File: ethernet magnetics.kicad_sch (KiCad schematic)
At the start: 3 parts

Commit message: wired phy controller
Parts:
- removed U?: ALANS10001-4J41ET, symbol local_library:ALANS10001-4J41ET
- added C? (x2): 6.8nF, symbol Device:C
- added C? (x2): 0.022uF, symbol Device:C
- added C?: 0.01uF, symbol Device:C
- added C?: 3.3uF, symbol Device:C_Polarized
- added C?: 1000pf, symbol Device:C
- added FB?: FerriteBead, symbol Device:FerriteBead
- added R? (x4): 49.9, symbol Device:R
- added R? (x2): 150R, symbol Device:R
- added R?: 10, symbol Device:R
- added T?: S558-5999-46-F, SOP254P1270X597-16N, symbol SamacSys_Parts:S558-5999-46-F
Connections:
- net ETH-RXn: now also R?.1, T?.6
- net ETH-RXp: now also R?.1, T?.7
- net ETH-TXn: now also T?.11
- net ETH-TXp: now also T?.10
- net MAG-RXn: now also C?.1, R?.1
- net MAG-RXp: now also C?.1, R?.1
- net MAG-TXn: now also R?.2, T?.15
- net MAG-TXp: now also R?.2, T?.16
- net at R?.1: now also T?.5
- net at R?.1: now also R?.2, C?.1, R?.2, R?.2
- net ETH-GND: no longer names the net of R?.2
- net ETH-GND: now also T?.12; no longer R?.2
- new net: C?.2, T?.1
- new net: C?.1, R?.2, R?.2, T?.3
- new net: C?.1, C?.1, FB?.2, R?.1, R?.1, R?.1
- new net: C?.1, R?.2, T?.14
- new net: C?.2, T?.2
- new net +3V3: FB?.1
- new net GND: C?.2, C?.2, C?.2, C?.2
- new net GND1: C?.2
- no-connect marks 0 -> 4
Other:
- moved on the sheet: R?

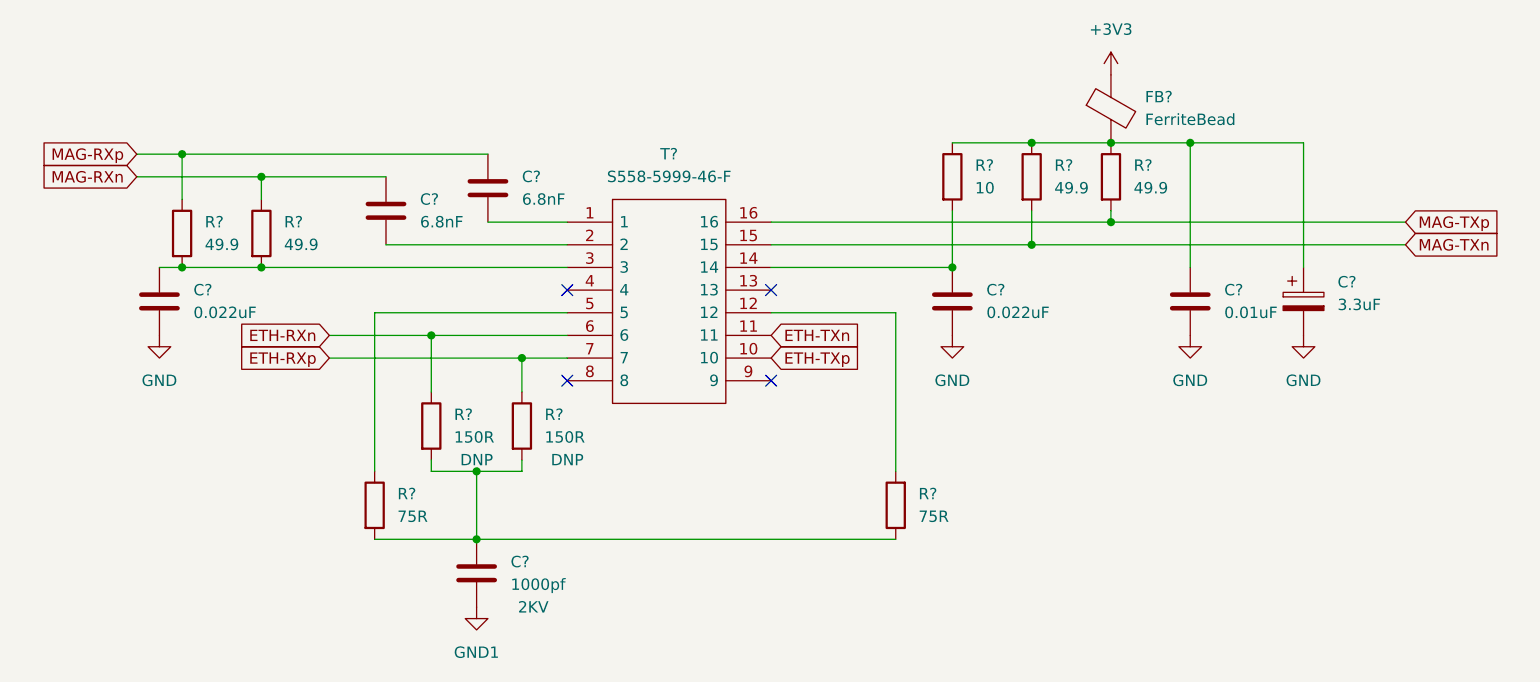
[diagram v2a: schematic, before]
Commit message: add component numbers to schematic
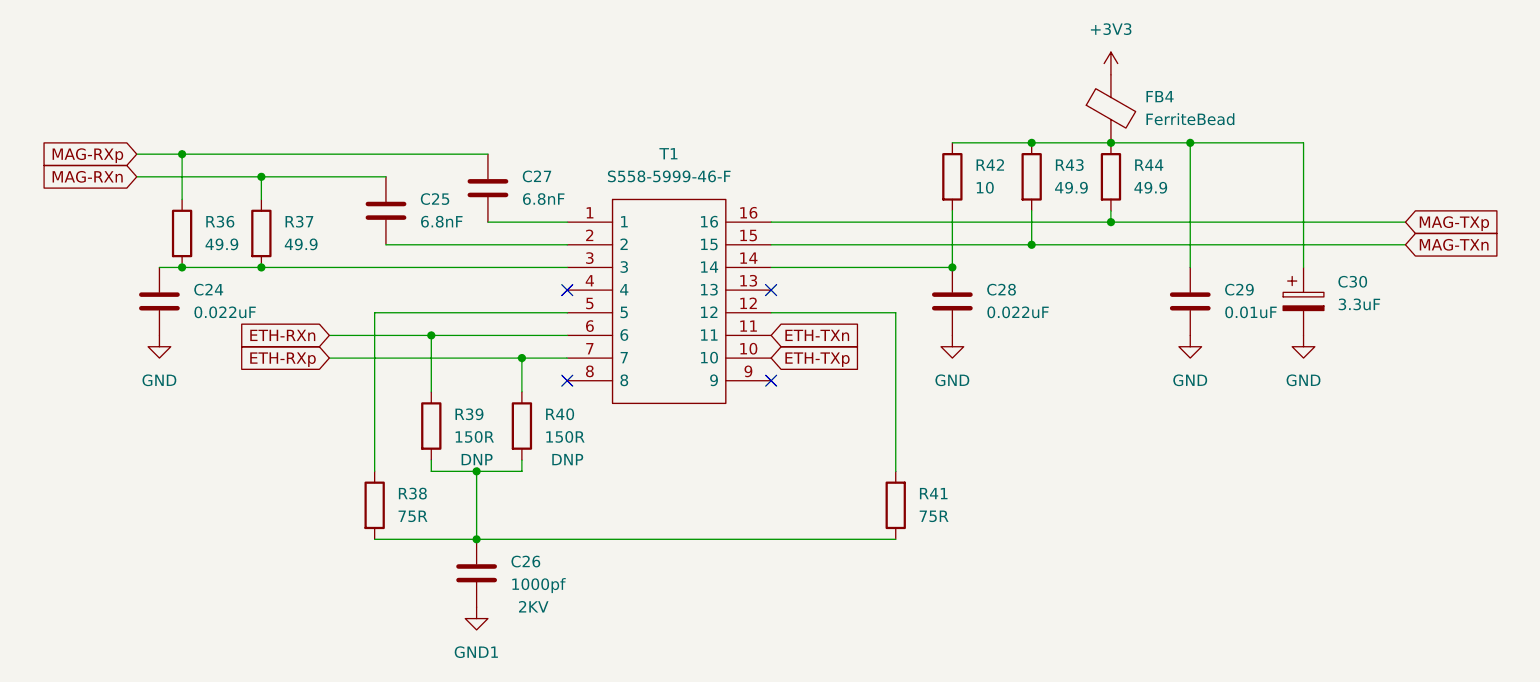
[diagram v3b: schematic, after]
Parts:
- gave numbers to parts that had none: 18
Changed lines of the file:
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@@
   (symbol (lib_id "power:GND") (at 199.39 85.09 0) (unit 1)
     (in_bom yes) (on_board yes) (fields_autoplaced)
-    (property "Reference" "#PWR?" (id 0) (at 199.39 91.44 0)
+    (property "Reference" "#PWR045" (id 0) (at 199.39 91.44 0)
       (effects (font (size 1.27 1.27)) hide)
     )
@@
   (symbol (lib_id "Device:C") (at 107.95 68.58 0) (unit 1)
     (in_bom yes) (on_board yes) (fields_autoplaced)
-    (property "Reference" "C?" (id 0) (at 111.76 67.3099 0)
+    (property "Reference" "C27" (id 0) (at 111.76 67.3099 0)
       (effects (font (size 1.27 1.27)) (justify left))
     )
@@
   (symbol (lib_id "Device:R") (at 95.25 104.14 0) (unit 1)
     (in_bom yes) (on_board yes) (fields_autoplaced)
-    (property "Reference" "R?" (id 0) (at 97.79 102.8699 0)
+    (property "Reference" "R38" (id 0) (at 97.79 102.8699 0)
       (effects (font (size 1.27 1.27)) (justify left))
     )
@@
   (symbol (lib_id "Device:C") (at 71.12 81.28 0) (unit 1)
     (in_bom yes) (on_board yes) (fields_autoplaced)
-    (property "Reference" "C?" (id 0) (at 74.93 80.0099 0)
+    (property "Reference" "C24" (id 0) (at 74.93 80.0099 0)
       (effects (font (size 1.27 1.27)) (justify left))
     )
@@
   (symbol (lib_id "Device:R") (at 177.8 67.31 0) (unit 1)
     (in_bom yes) (on_board yes) (fields_autoplaced)
-    (property "Reference" "R?" (id 0) (at 180.34 66.0399 0)
+    (property "Reference" "R44" (id 0) (at 180.34 66.0399 0)
       (effects (font (size 1.27 1.27)) (justify left))
     )
@@
   (symbol (lib_id "power:GND") (at 186.69 85.09 0) (unit 1)
     (in_bom yes) (on_board yes) (fields_autoplaced)
-    (property "Reference" "#PWR?" (id 0) (at 186.69 91.44 0)
+    (property "Reference" "#PWR044" (id 0) (at 186.69 91.44 0)
       (effects (font (size 1.27 1.27)) hide)
     )
@@
   (symbol (lib_id "Device:R") (at 73.66 73.66 0) (unit 1)
     (in_bom yes) (on_board yes) (fields_autoplaced)
-    (property "Reference" "R?" (id 0) (at 76.2 72.3899 0)
+    (property "Reference" "R36" (id 0) (at 76.2 72.3899 0)
       (effects (font (size 1.27 1.27)) (justify left))
     )
@@
   (symbol (lib_id "SamacSys_Parts:S558-5999-46-F") (at 116.84 72.39 0) (unit 1)
     (in_bom yes) (on_board yes) (fields_autoplaced)
-    (property "Reference" "T?" (id 0) (at 128.27 64.77 0))
+    (property "Reference" "T1" (id 0) (at 128.27 64.77 0))
     (property "Value" "S558-5999-46-F" (id 1) (at 128.27 67.31 0))
     (property "Footprint" "SOP254P1270X597-16N" (id 2) (at 135.89 69.85 0)
@@
   (symbol (lib_id "Device:C") (at 186.69 81.28 0) (unit 1)
     (in_bom yes) (on_board yes) (fields_autoplaced)
-    (property "Reference" "C?" (id 0) (at 190.5 80.0099 0)
+    (property "Reference" "C29" (id 0) (at 190.5 80.0099 0)
       (effects (font (size 1.27 1.27)) (justify left))
     )
@@
   (symbol (lib_id "Device:R") (at 111.76 95.25 0) (unit 1)
     (in_bom yes) (on_board yes)
-    (property "Reference" "R?" (id 0) (at 114.3 93.9799 0)
+    (property "Reference" "R40" (id 0) (at 114.3 93.9799 0)
       (effects (font (size 1.27 1.27)) (justify left))
     )
@@
   (symbol (lib_id "Device:R") (at 82.55 73.66 0) (unit 1)
     (in_bom yes) (on_board yes) (fields_autoplaced)
-    (property "Reference" "R?" (id 0) (at 85.09 72.3899 0)
+    (property "Reference" "R37" (id 0) (at 85.09 72.3899 0)
       (effects (font (size 1.27 1.27)) (justify left))
     )
@@
   (symbol (lib_id "Device:R") (at 168.91 67.31 0) (unit 1)
     (in_bom yes) (on_board yes) (fields_autoplaced)
-    (property "Reference" "R?" (id 0) (at 171.45 66.0399 0)
+    (property "Reference" "R43" (id 0) (at 171.45 66.0399 0)
       (effects (font (size 1.27 1.27)) (justify left))
     )
@@
   (symbol (lib_id "Device:C_Polarized") (at 199.39 81.28 0) (unit 1)
     (in_bom yes) (on_board yes) (fields_autoplaced)
-    (property "Reference" "C?" (id 0) (at 203.2 79.1209 0)
+    (property "Reference" "C30" (id 0) (at 203.2 79.1209 0)
       (effects (font (size 1.27 1.27)) (justify left))
     )
@@
   (symbol (lib_id "power:GND") (at 160.02 85.09 0) (unit 1)
     (in_bom yes) (on_board yes) (fields_autoplaced)
-    (property "Reference" "#PWR?" (id 0) (at 160.02 91.44 0)
+    (property "Reference" "#PWR042" (id 0) (at 160.02 91.44 0)
       (effects (font (size 1.27 1.27)) hide)
     )
@@
   (symbol (lib_id "power:+3V3") (at 177.8 55.88 0) (unit 1)
     (in_bom yes) (on_board yes) (fields_autoplaced)
-    (property "Reference" "#PWR?" (id 0) (at 177.8 59.69 0)
+    (property "Reference" "#PWR043" (id 0) (at 177.8 59.69 0)
       (effects (font (size 1.27 1.27)) hide)
     )
@@
   (symbol (lib_id "Device:R") (at 153.67 104.14 180) (unit 1)
     (in_bom yes) (on_board yes) (fields_autoplaced)
-    (property "Reference" "R?" (id 0) (at 156.21 102.8699 0)
+    (property "Reference" "R41" (id 0) (at 156.21 102.8699 0)
       (effects (font (size 1.27 1.27)) (justify right))
     )
@@
   (symbol (lib_id "Device:C") (at 96.52 71.12 0) (unit 1)
     (in_bom yes) (on_board yes) (fields_autoplaced)
-    (property "Reference" "C?" (id 0) (at 100.33 69.8499 0)
+    (property "Reference" "C25" (id 0) (at 100.33 69.8499 0)
       (effects (font (size 1.27 1.27)) (justify left))
     )
@@
   (symbol (lib_id "Device:C") (at 160.02 81.28 0) (unit 1)
     (in_bom yes) (on_board yes) (fields_autoplaced)
-    (property "Reference" "C?" (id 0) (at 163.83 80.0099 0)
+    (property "Reference" "C28" (id 0) (at 163.83 80.0099 0)
       (effects (font (size 1.27 1.27)) (justify left))
     )
@@
   (symbol (lib_id "power:GND") (at 71.12 85.09 0) (unit 1)
     (in_bom yes) (on_board yes) (fields_autoplaced)
-    (property "Reference" "#PWR?" (id 0) (at 71.12 91.44 0)
+    (property "Reference" "#PWR040" (id 0) (at 71.12 91.44 0)
       (effects (font (size 1.27 1.27)) hide)
     )
@@
   (symbol (lib_id "Device:R") (at 101.6 95.25 0) (unit 1)
     (in_bom yes) (on_board yes)
-    (property "Reference" "R?" (id 0) (at 104.14 93.9799 0)
+    (property "Reference" "R39" (id 0) (at 104.14 93.9799 0)
       (effects (font (size 1.27 1.27)) (justify left))
     )
@@
   (symbol (lib_id "power:GND1") (at 106.68 115.57 0) (unit 1)
     (in_bom yes) (on_board yes) (fields_autoplaced)
-    (property "Reference" "#PWR?" (id 0) (at 106.68 121.92 0)
+    (property "Reference" "#PWR041" (id 0) (at 106.68 121.92 0)
       (effects (font (size 1.27 1.27)) hide)
     )
@@
   (symbol (lib_id "Device:R") (at 160.02 67.31 0) (unit 1)
     (in_bom yes) (on_board yes) (fields_autoplaced)
-    (property "Reference" "R?" (id 0) (at 162.56 66.0399 0)
+    (property "Reference" "R42" (id 0) (at 162.56 66.0399 0)
       (effects (font (size 1.27 1.27)) (justify left))
     )
@@
   (symbol (lib_id "Device:C") (at 106.68 111.76 0) (unit 1)
     (in_bom yes) (on_board yes)
-    (property "Reference" "C?" (id 0) (at 110.49 110.4899 0)
+    (property "Reference" "C26" (id 0) (at 110.49 110.4899 0)
       (effects (font (size 1.27 1.27)) (justify left))
     )
@@
   (symbol (lib_id "Device:FerriteBead") (at 177.8 59.69 0) (unit 1)
     (in_bom yes) (on_board yes) (fields_autoplaced)
-    (property "Reference" "FB?" (id 0) (at 181.61 58.3691 0)
-      (effects (font (size 1.27 1.27)) (justify left))
-    )
+    (property "Reference" "FB4" (id 0) (at 181.61 58.3691 0)
+      (effects (font (size 1.27 1.27)) (justify left))
+    )

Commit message: Assign footprints to ICs
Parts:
- T1: footprint SOP254P1270X597-16N -> Magnetics:SOP254P1270X597-16N
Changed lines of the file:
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@@
     (property "Reference" "T1" (id 0) (at 128.27 64.77 0))
     (property "Value" "S558-5999-46-F" (id 1) (at 128.27 67.31 0))
-    (property "Footprint" "SOP254P1270X597-16N" (id 2) (at 135.89 69.85 0)
+    (property "Footprint" "Magnetics:SOP254P1270X597-16N" (id 2) (at 135.89 69.85 0)
       (effects (font (size 1.27 1.27)) (justify left) hide)
     )

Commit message: Resistor and cap footprints (except the ones the store cupboard doesn't have)
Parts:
- C24, C25, C26, C27, C28, C29: footprint (none) -> Capacitor_SMD:C_0603_1608Metric_Pad1.08x0.95mm_HandSolder
- C30: footprint (none) -> Capacitor_Tantalum_SMD:CP_EIA-6032-15_Kemet-U_Pad2.25x2.35mm_HandSolder
- R36, R37, R38, R39, R40, R41, R42, R43, R44: footprint (none) -> Resistor_SMD:R_0805_2012Metric_Pad1.20x1.40mm_HandSolder
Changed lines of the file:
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@@
       (effects (font (size 1.27 1.27)) (justify left))
     )
-    (property "Footprint" "" (id 2) (at 108.9152 72.39 0)
+    (property "Footprint" "Capacitor_SMD:C_0603_1608Metric_Pad1.08x0.95mm_HandSolder" (id 2) (at 108.9152 72.39 0)
       (effects (font (size 1.27 1.27)) hide)
     )
@@
       (effects (font (size 1.27 1.27)) (justify left))
     )
-    (property "Footprint" "" (id 2) (at 93.472 104.14 90)
+    (property "Footprint" "Resistor_SMD:R_0805_2012Metric_Pad1.20x1.40mm_HandSolder" (id 2) (at 93.472 104.14 90)
       (effects (font (size 1.27 1.27)) hide)
     )
@@
       (effects (font (size 1.27 1.27)) (justify left))
     )
-    (property "Footprint" "" (id 2) (at 72.0852 85.09 0)
+    (property "Footprint" "Capacitor_SMD:C_0603_1608Metric_Pad1.08x0.95mm_HandSolder" (id 2) (at 72.0852 85.09 0)
       (effects (font (size 1.27 1.27)) hide)
     )
@@
       (effects (font (size 1.27 1.27)) (justify left))
     )
-    (property "Footprint" "" (id 2) (at 176.022 67.31 90)
+    (property "Footprint" "Resistor_SMD:R_0805_2012Metric_Pad1.20x1.40mm_HandSolder" (id 2) (at 176.022 67.31 90)
       (effects (font (size 1.27 1.27)) hide)
     )
@@
       (effects (font (size 1.27 1.27)) (justify left))
     )
-    (property "Footprint" "" (id 2) (at 71.882 73.66 90)
+    (property "Footprint" "Resistor_SMD:R_0805_2012Metric_Pad1.20x1.40mm_HandSolder" (id 2) (at 71.882 73.66 90)
       (effects (font (size 1.27 1.27)) hide)
     )
@@
       (effects (font (size 1.27 1.27)) (justify left))
     )
-    (property "Footprint" "" (id 2) (at 187.6552 85.09 0)
+    (property "Footprint" "Capacitor_SMD:C_0603_1608Metric_Pad1.08x0.95mm_HandSolder" (id 2) (at 187.6552 85.09 0)
       (effects (font (size 1.27 1.27)) hide)
     )
@@
       (effects (font (size 1.27 1.27)) (justify left))
     )
-    (property "Footprint" "" (id 2) (at 109.982 95.25 90)
+    (property "Footprint" "Resistor_SMD:R_0805_2012Metric_Pad1.20x1.40mm_HandSolder" (id 2) (at 109.982 95.25 90)
       (effects (font (size 1.27 1.27)) hide)
     )
@@
       (effects (font (size 1.27 1.27)) (justify left))
     )
-    (property "Footprint" "" (id 2) (at 80.772 73.66 90)
+    (property "Footprint" "Resistor_SMD:R_0805_2012Metric_Pad1.20x1.40mm_HandSolder" (id 2) (at 80.772 73.66 90)
       (effects (font (size 1.27 1.27)) hide)
     )
@@
       (effects (font (size 1.27 1.27)) (justify left))
     )
-    (property "Footprint" "" (id 2) (at 167.132 67.31 90)
+    (property "Footprint" "Resistor_SMD:R_0805_2012Metric_Pad1.20x1.40mm_HandSolder" (id 2) (at 167.132 67.31 90)
       (effects (font (size 1.27 1.27)) hide)
     )
@@
       (effects (font (size 1.27 1.27)) (justify left))
     )
-    (property "Footprint" "" (id 2) (at 200.3552 85.09 0)
+    (property "Footprint" "Capacitor_Tantalum_SMD:CP_EIA-6032-15_Kemet-U_Pad2.25x2.35mm_HandSolder" (id 2) (at 200.3552 85.09 0)
       (effects (font (size 1.27 1.27)) hide)
     )
@@
       (effects (font (size 1.27 1.27)) (justify right))
     )
-    (property "Footprint" "" (id 2) (at 155.448 104.14 90)
+    (property "Footprint" "Resistor_SMD:R_0805_2012Metric_Pad1.20x1.40mm_HandSolder" (id 2) (at 155.448 104.14 90)
       (effects (font (size 1.27 1.27)) hide)
     )
@@
       (effects (font (size 1.27 1.27)) (justify left))
     )
-    (property "Footprint" "" (id 2) (at 97.4852 74.93 0)
+    (property "Footprint" "Capacitor_SMD:C_0603_1608Metric_Pad1.08x0.95mm_HandSolder" (id 2) (at 97.4852 74.93 0)
       (effects (font (size 1.27 1.27)) hide)
     )
@@
       (effects (font (size 1.27 1.27)) (justify left))
     )
-    (property "Footprint" "" (id 2) (at 160.9852 85.09 0)
+    (property "Footprint" "Capacitor_SMD:C_0603_1608Metric_Pad1.08x0.95mm_HandSolder" (id 2) (at 160.9852 85.09 0)
       (effects (font (size 1.27 1.27)) hide)
     )
@@
       (effects (font (size 1.27 1.27)) (justify left))
     )
-    (property "Footprint" "" (id 2) (at 99.822 95.25 90)
+    (property "Footprint" "Resistor_SMD:R_0805_2012Metric_Pad1.20x1.40mm_HandSolder" (id 2) (at 99.822 95.25 90)
       (effects (font (size 1.27 1.27)) hide)
     )
@@
       (effects (font (size 1.27 1.27)) (justify left))
     )
-    (property "Footprint" "" (id 2) (at 158.242 67.31 90)
+    (property "Footprint" "Resistor_SMD:R_0805_2012Metric_Pad1.20x1.40mm_HandSolder" (id 2) (at 158.242 67.31 90)
       (effects (font (size 1.27 1.27)) hide)
     )
@@
       (effects (font (size 1.27 1.27)) (justify left))
     )
-    (property "Footprint" "" (id 2) (at 107.6452 115.57 0)
-      (effects (font (size 1.27 1.27)) hide)
-    )
+    (property "Footprint" "Capacitor_SMD:C_0603_1608Metric_Pad1.08x0.95mm_HandSolder" (id 2) (at 107.6452 115.57 0)
+      (effects (font (size 1.27 1.27)) hide)
+    )

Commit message: Assign footprints to everything bar inductors
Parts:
- FB4: footprint (none) -> Inductor_SMD:L_1206_3216Metric_Pad1.22x1.90mm_HandSolder
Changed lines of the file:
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@@
       (effects (font (size 1.27 1.27)) (justify left))
     )
-    (property "Footprint" "" (id 2) (at 176.022 59.69 90)
+    (property "Footprint" "Inductor_SMD:L_1206_3216Metric_Pad1.22x1.90mm_HandSolder" (id 2) (at 176.022 59.69 90)
       (effects (font (size 1.27 1.27)) hide)
     )
